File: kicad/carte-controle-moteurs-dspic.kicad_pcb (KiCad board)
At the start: 4 copper layers, 137.2 x 81.3 mm, 73 parts, among them J1 PDB, J10 PWR_IN, J11 GND, J12 5V, J13 3.3V, J14 EN, J15 MOTEUR 1, J16 MOTEUR 2, J17 L1, J18 H1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

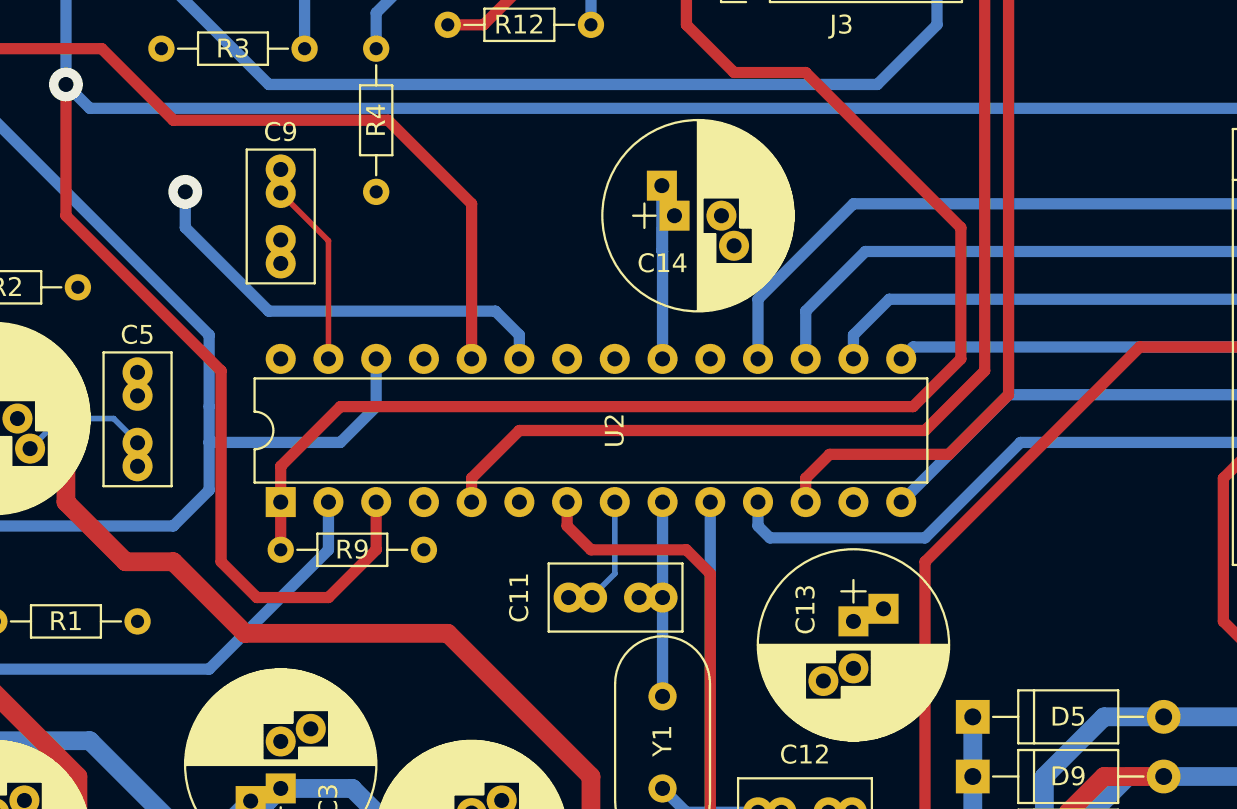
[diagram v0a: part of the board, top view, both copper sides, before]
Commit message: Ajout d'un lot de capacités pour la patte 28 du DsPIC
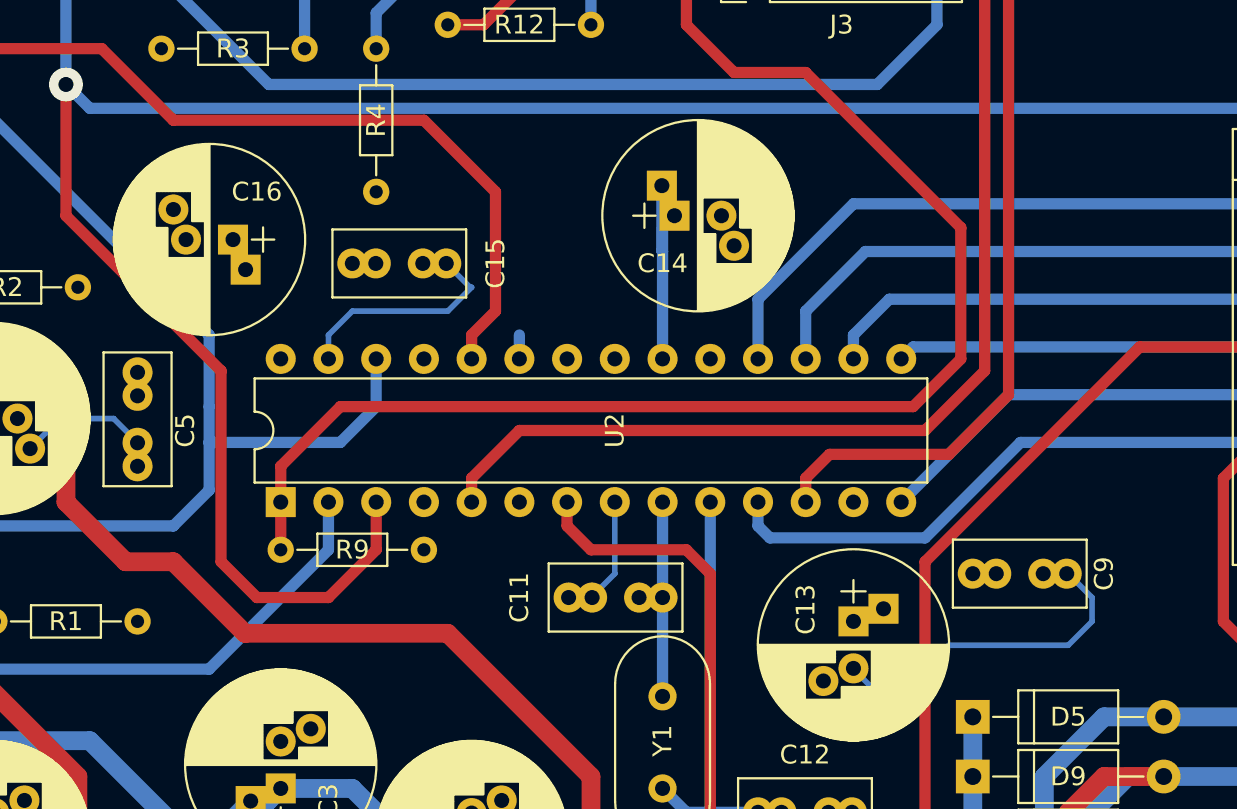
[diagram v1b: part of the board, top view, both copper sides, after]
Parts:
- added C15: 100n, Capacitors_THT:C_Rect_L7.0mm_W3.5mm_P2.50mm_P5.00mm, F.Cu at (81.3, 58.4)
- added C16: 1u, Capacitors_THT:CP_Radial_D10.0mm_P2.50mm_P5.00mm, F.Cu at (74.9, 57.1)
- moved C9 40.4 mm to (114.3, 74.9), turned to 0 degrees
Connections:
- J10 pad 4: (no net) -> Net-(J10-Pad4)
- J3 pad 1: (no net) -> Net-(J3-Pad1)
- J3 pad 3: (no net) -> Net-(J3-Pad3)
- J6 pad 1: (no net) -> Net-(J6-Pad1)
- J7 pad 1: (no net) -> Net-(J7-Pad1)
- J8 pad 1: (no net) -> Net-(J8-Pad1)
- J9 pad 1: (no net) -> Net-(J9-Pad1)
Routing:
- net GND: track 61.2 -> 82.3 mm
- net +3V3: track 28.1 -> 40.8 mm
- net /PWM1_H2: track 66.5 -> 71.1 mm, vias 1 -> 0
- net /PWM1_L2: track 70.0 -> 72.1 mm
- net /QEI1_INDEX: track 82.3 -> 83.8 mm
- net /PWM1_H1: track 75.7 -> 74.9 mm
